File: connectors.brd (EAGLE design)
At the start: 14.5 x 14.5 mm, 19 parts, among them CON2 PINHEAD_1X03-2.54-RA, CON3 CON-4P-JST_GH-RA, CON4 PINHEAD_1X02-2, CON5 PINHEAD_1X02-2, CON6 PINHEAD_1X07-2, CON8 CON-4P-JST_GH-RA, IC1 TPD3S014DBVR-SOT23-6, IC3 TJA1051

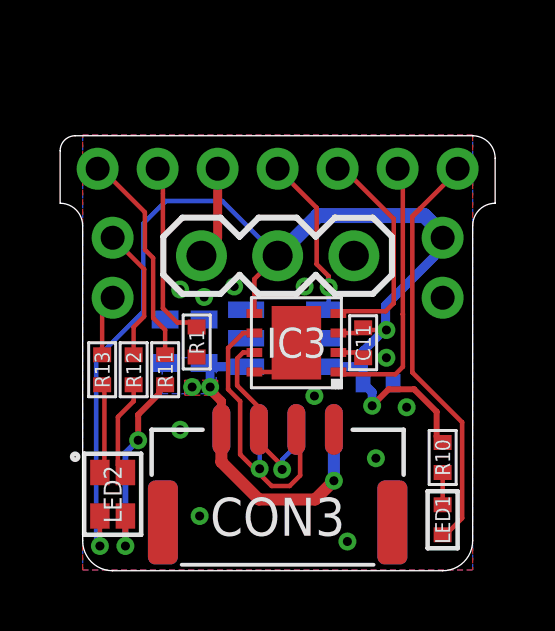
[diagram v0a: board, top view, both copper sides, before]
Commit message: connectors pcb outline update
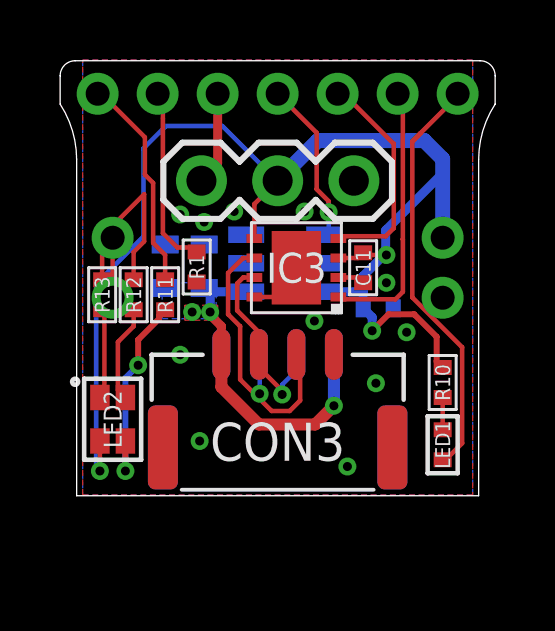
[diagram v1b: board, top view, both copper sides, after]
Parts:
- moved C11 2.50 mm to (2.85, 7.60)
- moved C3 2.50 mm to (3.35, 6.25)
- moved C5 2.50 mm to (-3.75, 7.65)
- moved C7 2.50 mm to (-2.45, 7.65)
- moved CON2 2.50 mm to (0.00, 10.5)
- moved CON3 2.50 mm to (0.00, 1.80)
- moved CON6 2.50 mm to (0.00, 13.4)
- moved CON8 2.50 mm to (0.00, 1.80)
- moved IC1 2.50 mm to (0.25, 7.75)
- moved IC3 2.50 mm to (0.62, 7.60)
- moved LED1 2.50 mm to (5.50, 1.70)
- moved LED2 2.50 mm to (-5.50, 2.55)
- moved R1 2.50 mm to (-2.70, 7.62)
- moved R10 2.50 mm to (5.50, 3.77)
- moved R11 2.50 mm to (-3.75, 6.70)
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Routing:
- net VDD_5V: track 40.4 -> 44.7 mm
- net RED: track 2.04 -> 3.84 mm
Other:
- outline, holes or cut-outs redrawn

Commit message: update
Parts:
- moved C11 2.50 mm to (2.85, 5.10)
- moved C3 2.50 mm to (3.35, 3.75)
- moved C5 2.50 mm to (-3.75, 5.15)
- moved C7 2.50 mm to (-2.45, 5.15)
- moved CON2 2.50 mm to (0.00, 8.00)
- moved CON3 2.50 mm to (0.00, -0.70)
- moved CON6 2.50 mm to (0.00, 10.9)
- moved CON8 2.50 mm to (0.00, -0.70)
- moved IC1 2.50 mm to (0.25, 5.25)
- moved IC3 2.50 mm to (0.62, 5.10)
- moved LED1 2.50 mm to (5.50, -0.80)
- moved LED2 2.50 mm to (-5.50, 0.05)
- moved R1 2.50 mm to (-2.70, 5.12)
- moved R10 2.50 mm to (5.50, 1.27)
- moved R11 2.50 mm to (-3.75, 4.20)
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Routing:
- net VDD_5V: track 44.7 -> 40.4 mm
- net RED: track 3.84 -> 2.04 mm
